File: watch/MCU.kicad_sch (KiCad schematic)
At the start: 14 parts, among them IC601 FAN5622SX, IC602 USBLC6-2P6, IC603 MX25U51245GZ4I00, IC604 NTS0104GU12, M601 NORA-B106, X603 Device, X608 Display

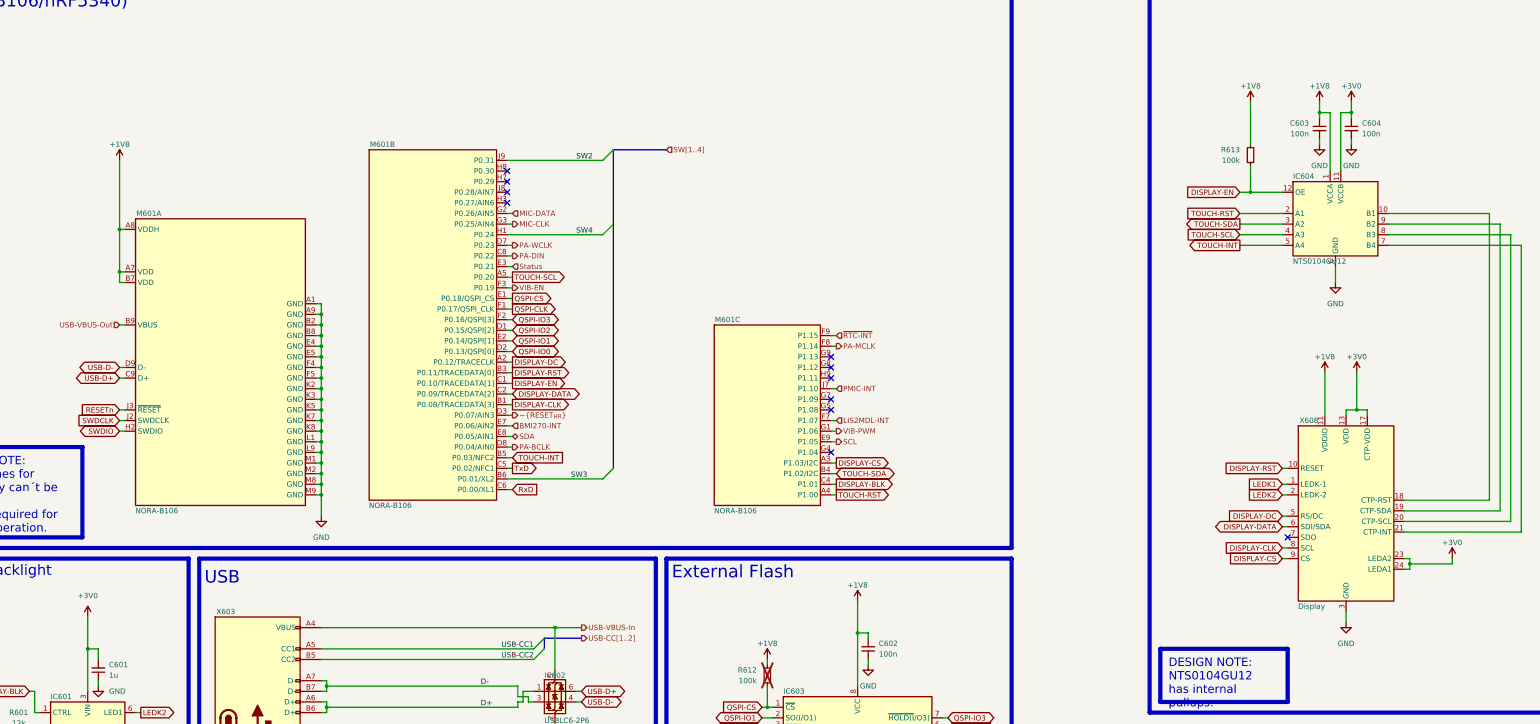
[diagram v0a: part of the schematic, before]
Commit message: Bug: Issue #14
- Change 3V0 to 3V3 to prevent flickering display

Closes: #14

Signed-off-by: Daniel Kampert <DanielKampert@kampis-elektroecke.de>
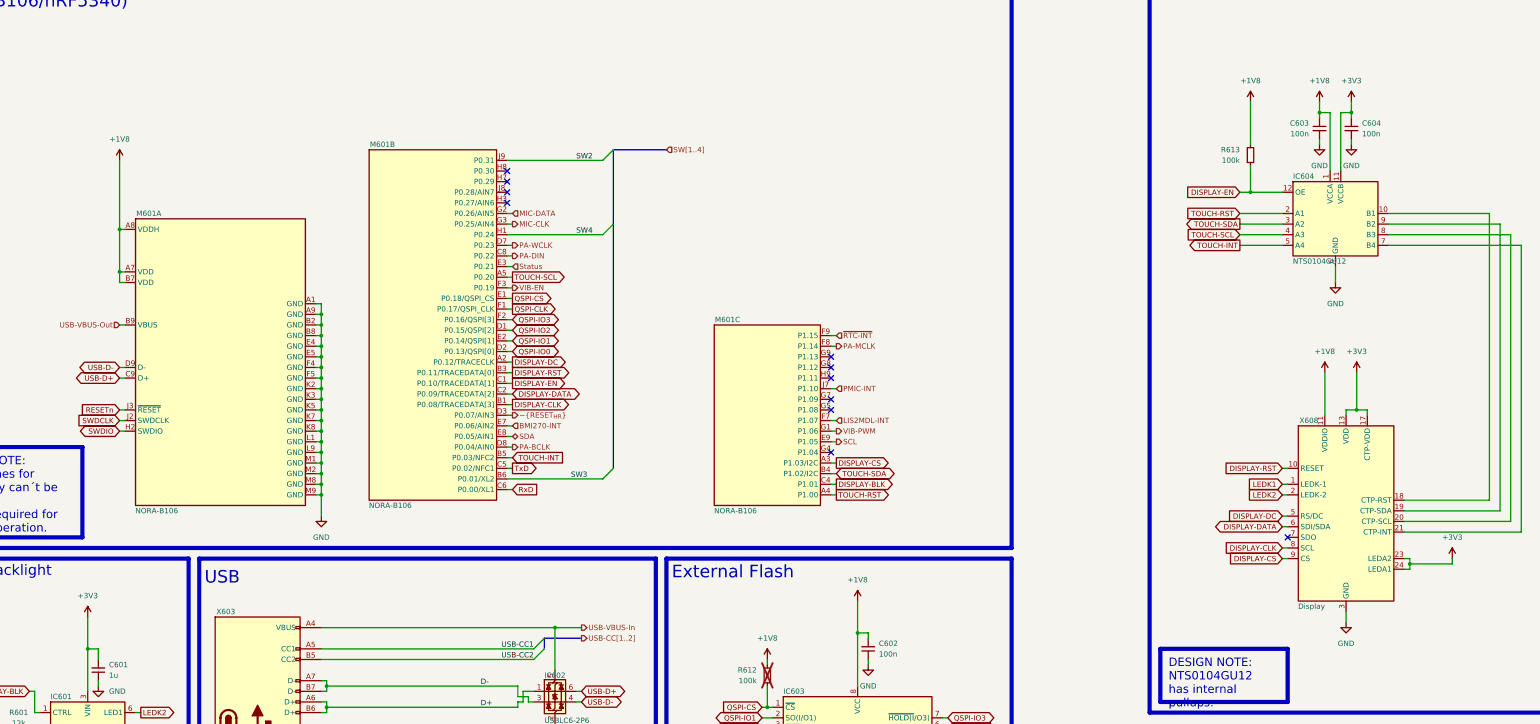
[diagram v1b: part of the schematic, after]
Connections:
- net +3V0 renamed +3V3
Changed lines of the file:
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@@
 		(dnp no)
 		(fields_autoplaced yes)
-		(property "Reference" "#PWR0615"
+		(property "Reference" "#PWR615"
 			(at 215.9 185.42 0)
 			(effects
@@
 		)
 		(property "Value" "+1V8"
-			(at 215.9 177.8 0)
+			(at 215.9 176.53 0)
 			(effects
 				(font
@@
 			(project "ZSWatch"
 				(path "/d5742f03-3b1a-42e5-a384-018bd4b919aa/c5103ceb-5325-4a84-a025-9638a412984e/8c9f2ee7-84da-4a9a-b0dc-117e0b0a9ea7"
-					(reference "#PWR0615")
+					(reference "#PWR615")
 					(unit 1)
 				)
@@
 		(dnp no)
 		(fields_autoplaced yes)
-		(property "Reference" "#PWR0608"
+		(property "Reference" "#PWR608"
 			(at 60.96 66.04 0)
 			(effects
@@
 		)
 		(property "Value" "+1V8"
-			(at 60.96 58.42 0)
+			(at 60.96 57.15 0)
 			(effects
 				(font
@@
 			(project "ZSWatch"
 				(path "/d5742f03-3b1a-42e5-a384-018bd4b919aa/c5103ceb-5325-4a84-a025-9638a412984e/8c9f2ee7-84da-4a9a-b0dc-117e0b0a9ea7"
-					(reference "#PWR0608")
+					(reference "#PWR608")
 					(unit 1)
 				)
@@
 		(dnp no)
 		(fields_autoplaced yes)
-		(property "Reference" "#PWR0621"
+		(property "Reference" "#PWR621"
 			(at 331.47 52.07 0)
 			(effects
@@
 		)
 		(property "Value" "+1V8"
-			(at 331.47 44.45 0)
+			(at 331.47 43.18 0)
 			(effects
 				(font
@@
 			(project "Dev-Kit"
 				(path "/d5742f03-3b1a-42e5-a384-018bd4b919aa/c5103ceb-5325-4a84-a025-9638a412984e/8c9f2ee7-84da-4a9a-b0dc-117e0b0a9ea7"
-					(reference "#PWR0621")
+					(reference "#PWR621")
 					(unit 1)
 				)
@@
 	)
 	(symbol
-		(lib_id "power:+3V0")
+		(lib_id "power:+3V3")
 		(at 379.73 157.48 0)
 		(unit 1)
@@
 		(dnp no)
 		(fields_autoplaced yes)
-		(property "Reference" "#PWR0631"
+		(property "Reference" "#PWR631"
 			(at 379.73 161.29 0)
 			(effects
@@
 			)
 		)
-		(property "Value" "+3V0"
-			(at 379.73 153.67 0)
+		(property "Value" "+3V3"
+			(at 379.73 152.4 0)
 			(effects
 				(font
@@
 			)
 		)
-		(property "Description" "Power symbol creates a global label with name \"+3V0\""
+		(property "Description" "Power symbol creates a global label with name \"+3V3\""
+			(at 379.73 157.48 0)
+			(effects
+				(font
+					(size 1.27 1.27)
+				)
+				(hide yes)
+			)
+		)
+		(property "manf" ""
+			(at 379.73 157.48 0)
+			(effects
+				(font
+					(size 1.27 1.27)
+				)
+				(hide yes)
+			)
+		)
+		(property "manf#" ""
+			(at 379.73 157.48 0)
+			(effects
+				(font
+					(size 1.27 1.27)
+				)
+				(hide yes)
+			)
+		)
+		(property "mouser#" ""
 			(at 379.73 157.48 0)
 			(effects
@@
 			(project "Dev-Kit"
 				(path "/d5742f03-3b1a-42e5-a384-018bd4b919aa/c5103ceb-5325-4a84-a025-9638a412984e/8c9f2ee7-84da-4a9a-b0dc-117e0b0a9ea7"
-					(reference "#PWR0631")
+					(reference "#PWR631")
 					(unit 1)
 				)
@@
 	)
 	(symbol
-		(lib_id "power:+3V0")
+		(lib_id "power:+3V3")
 		(at 53.34 171.45 0)
 		(unit 1)
@@
 		(dnp no)
 		(fields_autoplaced yes)
-		(property "Reference" "#PWR0605"
+		(property "Reference" "#PWR605"
 			(at 53.34 175.26 0)
 			(effects
@@
 			)
 		)
-		(property "Value" "+3V0"
+		(property "Value" "+3V3"
 			(at 53.34 166.37 0)
 			(effects
@@
 			)
 		)
-		(property "Description" "Power symbol creates a global label with name \"+3V0\""
+		(property "Description" "Power symbol creates a global label with name \"+3V3\""
 			(at 53.34 171.45 0)
 			(effects
@@
 			(project "Watch-DK"
 				(path "/d5742f03-3b1a-42e5-a384-018bd4b919aa/c5103ceb-5325-4a84-a025-9638a412984e/8c9f2ee7-84da-4a9a-b0dc-117e0b0a9ea7"
-					(reference "#PWR0605")
+					(reference "#PWR605")
 					(unit 1)
 				)
@@
 	)
 	(symbol
-		(lib_id "power:+3V0")
+		(lib_id "power:+3V3")
 		(at 355.6 48.26 0)
 		(unit 1)
@@
 		(dnp no)
 		(fields_autoplaced yes)
-		(property "Reference" "#PWR0628"
+		(property "Reference" "#PWR628"
 			(at 355.6 52.07 0)
 			(effects
@@
 			)
 		)
-		(property "Value" "+3V0"
-			(at 355.6 44.45 0)
+		(property "Value" "+3V3"
+			(at 355.6 43.18 0)
 			(effects
 				(font
@@
 			)
 		)
-		(property "Description" "Power symbol creates a global label with name \"+3V0\""
+		(property "Description" "Power symbol creates a global label with name \"+3V3\""
+			(at 355.6 48.26 0)
+			(effects
+				(font
+					(size 1.27 1.27)
+				)
+				(hide yes)
+			)
+		)
+		(property "manf" ""
+			(at 355.6 48.26 0)
+			(effects
+				(font
+					(size 1.27 1.27)
+				)
+				(hide yes)
+			)
+		)
+		(property "manf#" ""
+			(at 355.6 48.26 0)
+			(effects
+				(font
+					(size 1.27 1.27)
+				)
+				(hide yes)
+			)
+		)
+		(property "mouser#" ""
 			(at 355.6 48.26 0)
 			(effects
@@
 			(project "Dev-Kit"
 				(path "/d5742f03-3b1a-42e5-a384-018bd4b919aa/c5103ceb-5325-4a84-a025-9638a412984e/8c9f2ee7-84da-4a9a-b0dc-117e0b0a9ea7"
-					(reference "#PWR0628")
+					(reference "#PWR628")
 					(unit 1)
 				)
@@
 		(on_board yes)
 		(dnp no)
-		(property "Reference" "#PWR0625"
+		(fields_autoplaced yes)
+		(property "Reference" "#PWR625"
 			(at 349.25 116.84 0)
 			(effects
@@
 		)
 		(property "Value" "+1V8"
-			(at 349.25 109.22 0)
+			(at 349.25 107.95 0)
 			(effects
 				(font
@@
 			)
 		)
+		(property "manf" ""
+			(at 349.25 113.03 0)
+			(effects
+				(font
+					(size 1.27 1.27)
+				)
+				(hide yes)
+			)
+		)
+		(property "manf#" ""
+			(at 349.25 113.03 0)
+			(effects
+				(font
+					(size 1.27 1.27)
+				)
+				(hide yes)
+			)
+		)
+		(property "mouser#" ""
+			(at 349.25 113.03 0)
+			(effects
+				(font
+					(size 1.27 1.27)
+				)
+				(hide yes)
+			)
+		)
 		(pin "1"
 		)
@@
 			(project "ZSWatch"
 				(path "/d5742f03-3b1a-42e5-a384-018bd4b919aa/c5103ceb-5325-4a84-a025-9638a412984e/8c9f2ee7-84da-4a9a-b0dc-117e0b0a9ea7"
-					(reference "#PWR0625")
+					(reference "#PWR625")
 					(unit 1)
 				)
@@
 		(dnp no)
 		(fields_autoplaced yes)
-		(property "Reference" "#PWR0623"
+		(property "Reference" "#PWR623"
 			(at 347.98 52.07 0)
 			(effects
@@
 		)
 		(property "Value" "+1V8"
-			(at 347.98 44.45 0)
+			(at 347.98 43.18 0)
 			(effects
 				(font
@@
 			)
 		)
+		(property "manf" ""
+			(at 347.98 48.26 0)
+			(effects
+				(font
+					(size 1.27 1.27)
+				)
+				(hide yes)
+			)
+		)
+		(property "manf#" ""
+			(at 347.98 48.26 0)
+			(effects
+				(font
+					(size 1.27 1.27)
+				)
+				(hide yes)
+			)
+		)
+		(property "mouser#" ""
+			(at 347.98 48.26 0)
+			(effects
+				(font
+					(size 1.27 1.27)
+				)
+				(hide yes)
+			)
+		)
 		(pin "1"
 		)
@@
 			(project "ZSWatch"
 				(path "/d5742f03-3b1a-42e5-a384-018bd4b919aa/c5103ceb-5325-4a84-a025-9638a412984e/8c9f2ee7-84da-4a9a-b0dc-117e0b0a9ea7"
-					(reference "#PWR0623")
+					(reference "#PWR623")
 					(unit 1)
 				)
@@
 		(dnp no)
 		(fields_autoplaced yes)
-		(property "Reference" "#PWR0618"
+		(property "Reference" "#PWR618"
 			(at 237.49 171.45 0)
 			(effects
@@
 		)
 		(property "Value" "+1V8"
-			(at 237.49 163.83 0)
+			(at 237.49 162.56 0)
 			(effects
 				(font
@@
 			(project "ZSWatch"
 				(path "/d5742f03-3b1a-42e5-a384-018bd4b919aa/c5103ceb-5325-4a84-a025-9638a412984e/8c9f2ee7-84da-4a9a-b0dc-117e0b0a9ea7"
-					(reference "#PWR0618")
+					(reference "#PWR618")
 					(unit 1)
 				)
@@
 	)
 	(symbol
-		(lib_id "power:+3V0")
+		(lib_id "power:+3V3")
 		(at 356.87 113.03 0)
 		(unit 1)
@@
 		(dnp no)
 		(fields_autoplaced yes)
-		(property "Reference" "#PWR0630"
+		(property "Reference" "#PWR630"
 			(at 356.87 116.84 0)
 			(effects
@@
 			)
 		)
-		(property "Value" "+3V0"
-			(at 356.87 109.22 0)
+		(property "Value" "+3V3"
+			(at 356.87 107.95 0)
 			(effects
 				(font
@@
 			)
 		)
-		(property "Description" "Power symbol creates a global label with name \"+3V0\""
+		(property "Description" "Power symbol creates a global label with name \"+3V3\""
 			(at 356.87 113.03 0)
 			(effects
@@
 			(project "Dev-Kit"
 				(path "/d5742f03-3b1a-42e5-a384-018bd4b919aa/c5103ceb-5325-4a84-a025-9638a412984e/8c9f2ee7-84da-4a9a-b0dc-117e0b0a9ea7"
-					(reference "#PWR0630")
+					(reference "#PWR630")
 					(unit 1)
 				)
